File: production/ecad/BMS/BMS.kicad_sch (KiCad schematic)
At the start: 13 parts, among them J7 Conn_01x02_Pin, J8 XT60PW-M, J9 Conn_01x02_Pin, U2 AZ1117IH-3.3TRG1

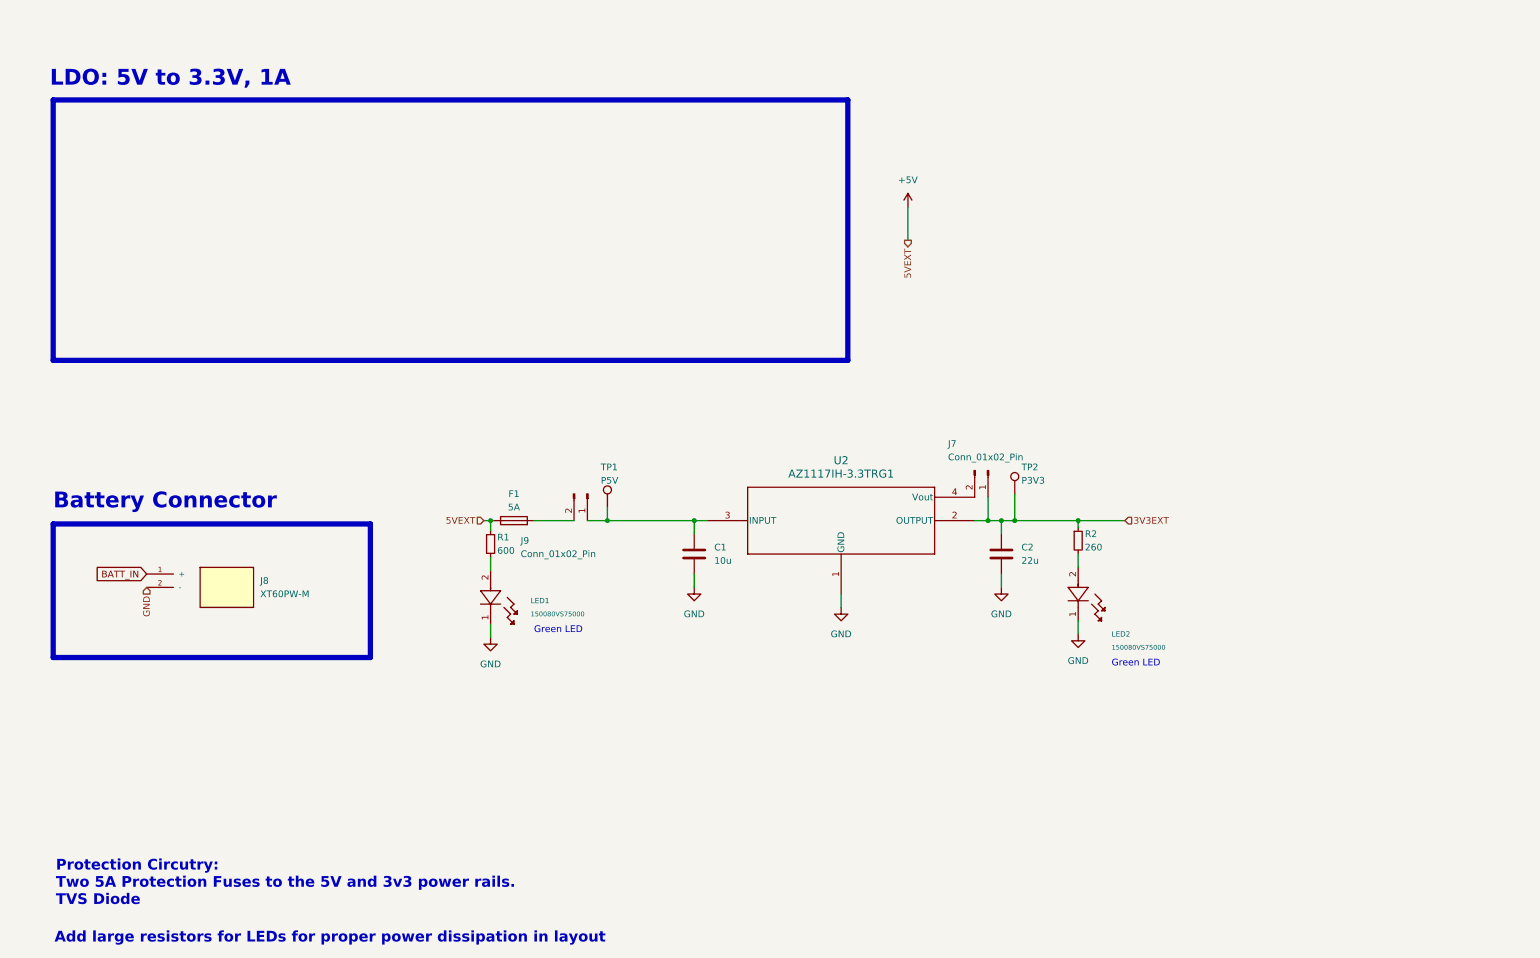
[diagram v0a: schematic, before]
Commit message: Updated LDO schematic
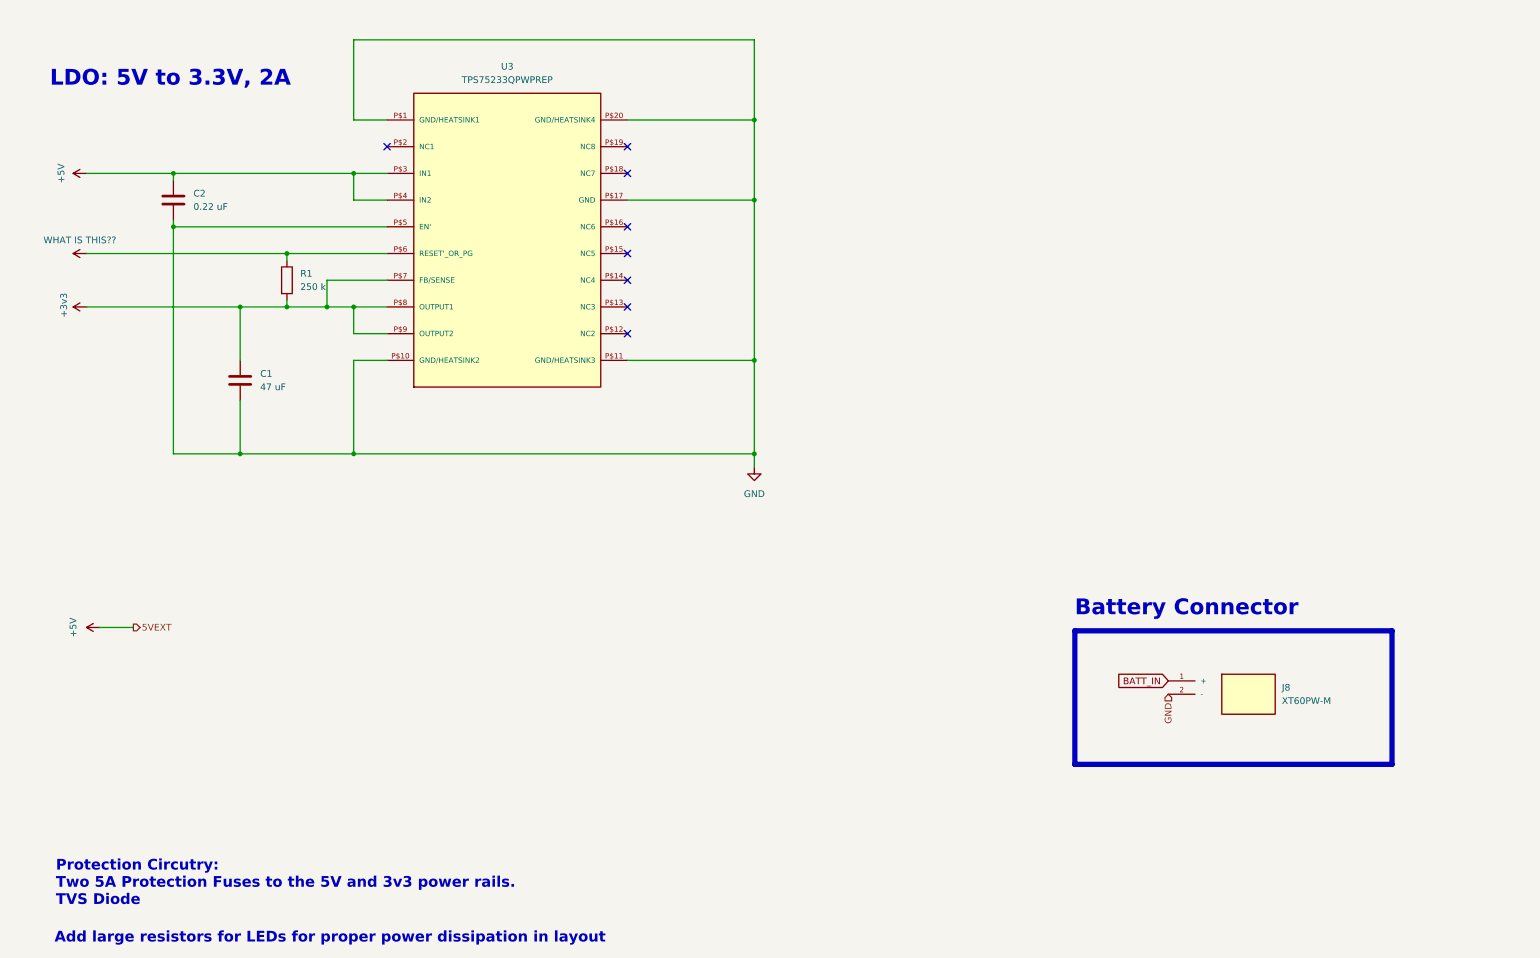
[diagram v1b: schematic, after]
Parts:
- removed F1: 5A, Fuse:Fuse_0805_2012Metric, symbol Device:Fuse
- removed J7, J9: Conn_01x02_Pin, Connector_PinHeader_2.54mm:PinHeader_1x02_P2.54mm_Vertical, symbol Connector:Conn_01x02_Pin
- removed LED1, LED2: 150080VS75000, CSTAR-MainBoard-Footprints:LED_0VS75000_WRE, symbol 2024-02-25_19-51-49:150080VS75000
- removed R1: 600, Resistor_SMD:R_0805_2012Metric, symbol Device:R_Small
- removed R2: 260, Resistor_SMD:R_0805_2012Metric, symbol Device:R_Small
- removed TP1: P5V, TestPoint:TestPoint_Pad_D2.0mm, symbol Connector:TestPoint
- removed TP2: P3V3, TestPoint:TestPoint_Pad_D2.0mm, symbol Connector:TestPoint
- removed U2: AZ1117IH-3.3TRG1, CSTAR-MainBoard-Footprints:SOT230P700X185-4N, symbol 2024-02-15_17-38-45:AZ1117IH-3.3TRG1
- added R1: 250 k, symbol Device:R
- added U3: TPS75233QPWPREP, TPS75233QPWPREP:TPS75233QPWPREP, symbol TPS75233QPWPREP:TPS75233QPWPREP
- C1: value 10u -> 47 uF; footprint Capacitor_SMD:C_0805_2012Metric -> (none)
- C2: value 22u -> 0.22 uF; footprint Capacitor_SMD:C_0805_2012Metric -> (none)
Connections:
- net 3V3EXT is gone; now on net +5V: C2.1
- net +5V: now also U3.P$3 (IN1), U3.P$4 (IN2)
- net GND: now also U3.P$1 (GND/HEATSINK1), U3.P$10 (GND/HEATSINK2), U3.P$11 (GND/HEATSINK3), U3.P$17 (GND), U3.P$20 (GND/HEATSINK4), U3.P$5 (EN')
- net +3v3: now reaches C1.1
- net +3v3: now also R1.2, U3.P$7 (FB/SENSE), U3.P$8 (OUTPUT1), U3.P$9 (OUTPUT2)
- new net WHAT IS THIS??: R1.1, U3.P$6 (RESET'_OR_PG)
- no-connect marks 0 -> 8
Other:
- note added: "LDO: 5V to 3.3V, 2A"
- note removed: "Green LED"
- note removed: "LDO: 5V to 3.3V, 1A"
- moved on the sheet: J8

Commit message: updated pullup resistors
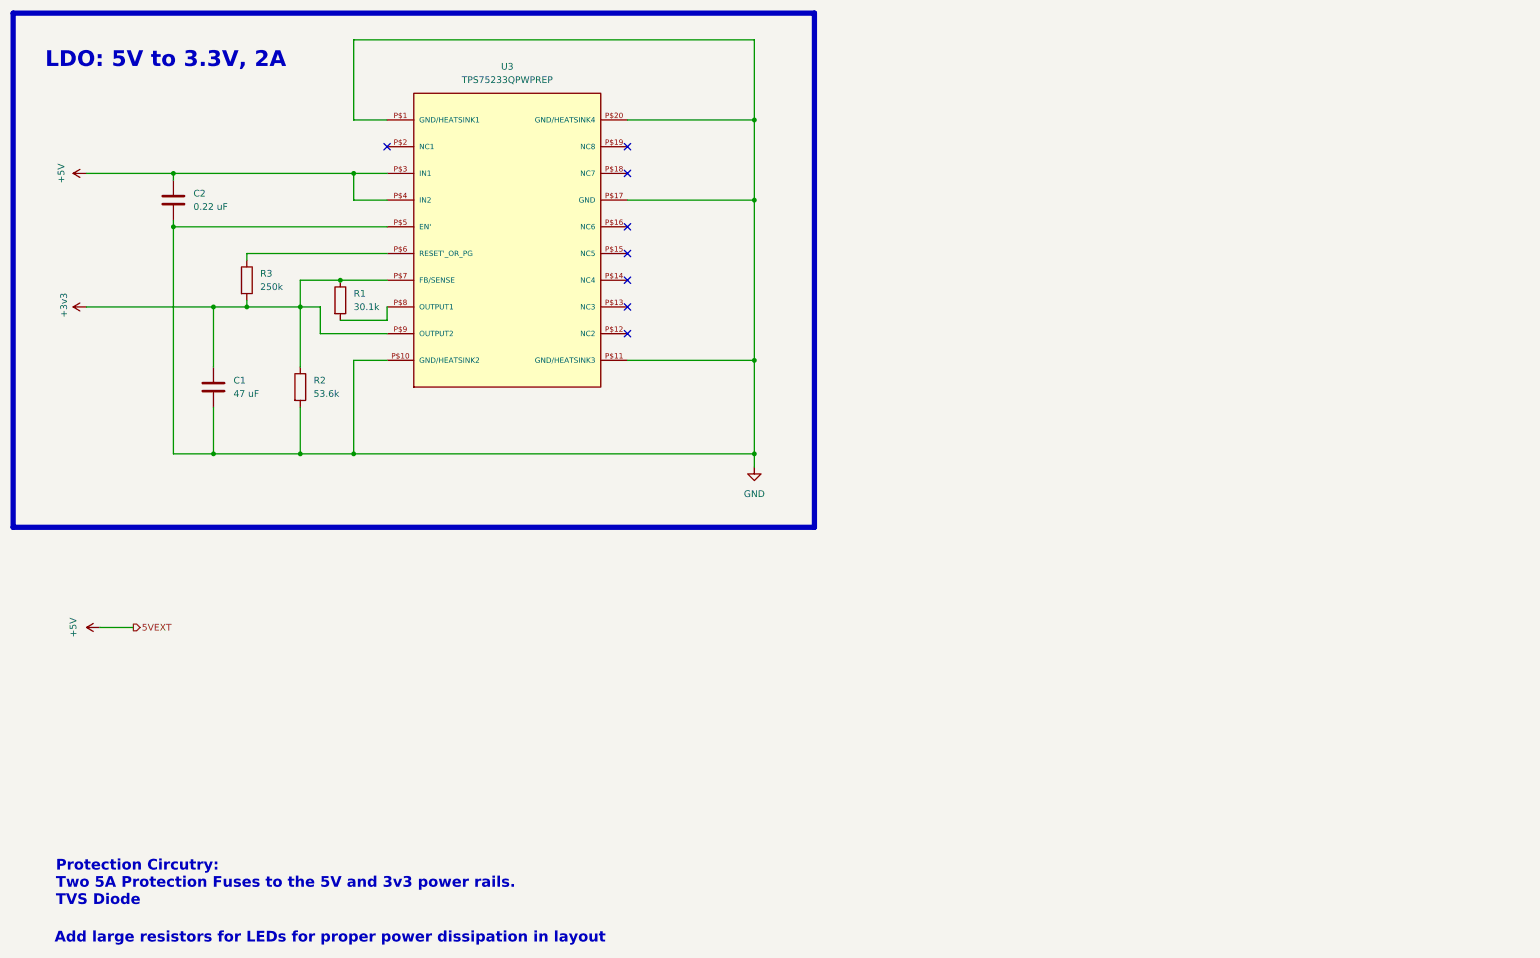
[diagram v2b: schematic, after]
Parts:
- removed J8: XT60PW-M, CSTAR-MainBoard-Footprints:AMASS_XT60PW-M, symbol XT60PW-M:XT60PW-M
- added R1: 30.1k, symbol Device:R
- added R2: 53.6k, symbol Device:R
- R3: renamed from R1; value 250 k -> 250k
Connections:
- net +3v3: now also R1.1, R2.1; no longer U3.P$8 (OUTPUT1)
- net GND: now also R2.2
- net WHAT IS THIS??: no longer names the net of R3.1, U3.P$6 (RESET'_OR_PG)
- new net: R1.2, U3.P$8 (OUTPUT1)
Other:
- note removed: "Battery Connector"
- moved on the sheet: C1, R3

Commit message: erc check
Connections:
- net +3v3 renamed +3V3

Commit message: barreljack
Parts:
- added J7: ADC-028-1-T/R-PA10T, ADC-028-x-T/R-PA10T_ADM, symbol 2024-10-20_20-22-38:ADC-028-1-T_R-PA10T
- R1: value 30.1k -> 53.6k
- R2: value 53.6k -> 30.1k
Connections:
- net +3V3: now also R1.2, U3.P$8 (OUTPUT1)
- net +5V: now also J7.2
- net GND: now also J7.1A
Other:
- note added: "Barrel jack connector: 5V from wall adapter"
- moved on the sheet: C1, C2, R1, R2, R3, U3

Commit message: erc
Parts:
- renumbered R3 to R8, U3 to U4
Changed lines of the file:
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@@
 		(dnp no)
 		(fields_autoplaced yes)
-		(property "Reference" "R3"
+		(property "Reference" "R8"
 			(at 71.12 66.0399 0)
 			(effects
@@
 			(project "Main"
 				(path "/a34d77bc-8f6a-417e-a206-3165e6c5c658/8907b1b2-1248-4544-8d7d-33764869f691"
-					(reference "R3")
+					(reference "R8")
 					(unit 1)
 				)
@@
 		(dnp no)
 		(fields_autoplaced yes)
-		(property "Reference" "U3"
+		(property "Reference" "U4"
 			(at 118.11 26.67 0)
 			(effects
@@
 			(project "Main"
 				(path "/a34d77bc-8f6a-417e-a206-3165e6c5c658/8907b1b2-1248-4544-8d7d-33764869f691"
-					(reference "U3")
+					(reference "U4")
 					(unit 1)
 				)

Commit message: Stylistic changes made
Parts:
- added R10, R9: 0, symbol Device:R
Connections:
- net +5V: now also J7.3, R10.2; no longer J7.2
- net GND: now also R9.2; no longer U4.P$1 (GND/HEATSINK1), U4.P$5 (EN')
- net at J7.1B: now also R9.1
- new net: J7.2, R10.1

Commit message: Stylistic edits made
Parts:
- renumbered R10 to DNP
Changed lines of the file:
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@@
 	(hierarchical_label "5VEXT"
 		(shape input)
-		(at 38.1 46.99 180)
+		(at 196.85 99.06 180)
 		(fields_autoplaced yes)
 		(effects
@@
 	(hierarchical_label "3V3EXT"
 		(shape input)
-		(at 38.1 72.39 180)
+		(at 196.85 105.41 180)
 		(fields_autoplaced yes)
 		(effects
@@
 		)
 	)
-	(hierarchical_label "5VEXT"
+	(hierarchical_label "GND"
 		(shape input)
-		(at 196.85 99.06 180)
+		(at 199.39 85.09 180)
 		(fields_autoplaced yes)
 		(effects
@@
 		)
 	)
-	(hierarchical_label "3V3EXT"
-		(shape input)
-		(at 196.85 105.41 180)
-		(fields_autoplaced yes)
-		(effects
-			(font
-				(size 1.27 1.27)
-			)
-			(justify right)
-		)
-	)
-	(hierarchical_label "GND"
-		(shape input)
-		(at 199.39 85.09 180)
-		(fields_autoplaced yes)
-		(effects
-			(font
-				(size 1.27 1.27)
-			)
-			(justify right)
-		)
-	)
 	(symbol
 		(lib_id "2024-10-20_20-22-38:ADC-028-1-T_R-PA10T")
@@
 	)
 	(symbol
+		(lib_id "power:+3V3")
+		(at 38.1 72.39 0)
+		(unit 1)
+		(exclude_from_sim no)
+		(in_bom yes)
+		(on_board yes)
+		(dnp no)
+		(fields_autoplaced yes)
+		(property "Reference" "#PWR045"
+			(at 38.1 76.2 0)
+			(effects
+				(font
+					(size 1.27 1.27)
+				)
+				(hide yes)
+			)
+		)
+		(property "Value" "+3V3"
+			(at 40.64 71.1199 0)
+			(effects
+				(font
+					(size 1.27 1.27)
+				)
+				(justify left)
+			)
+		)
+		(property "Footprint" ""
+			(at 38.1 72.39 0)
+			(effects
+				(font
+					(size 1.27 1.27)
+				)
+				(hide yes)
+			)
+		)
+		(property "Datasheet" ""
+			(at 38.1 72.39 0)
+			(effects
+				(font
+					(size 1.27 1.27)
+				)
+				(hide yes)
+			)
+		)
+		(property "Description" "Power symbol creates a global label with name \"+3V3\""
+			(at 38.1 72.39 0)
+			(effects
+				(font
+					(size 1.27 1.27)
+				)
+				(hide yes)
+			)
+		)
+		(pin "1"
+		)
+		(instances
+			(project "Main"
+				(path "/a34d77bc-8f6a-417e-a206-3165e6c5c658/8907b1b2-1248-4544-8d7d-33764869f691"
+					(reference "#PWR045")
+					(unit 1)
+				)
+			)
+		)
+	)
+	(symbol
 		(lib_id "power:GND")
 		(at 90.17 82.55 0)
@@
 		(on_board yes)
 		(dnp no)
-		(property "Reference" "R10"
+		(property "Reference" "DNP"
 			(at 231.394 48.006 90)
 			(effects
@@
 			(project "Main"
 				(path "/a34d77bc-8f6a-417e-a206-3165e6c5c658/8907b1b2-1248-4544-8d7d-33764869f691"
-					(reference "R10")
-					(unit 1)
-				)
+					(reference "DNP")
+					(unit 1)
+				)
+			)
+		)
+	)
+	(symbol
+		(lib_id "power:+5V")
+		(at 38.1 46.99 0)
+		(unit 1)
+		(exclude_from_sim no)
+		(in_bom yes)
+		(on_board yes)
+		(dnp no)
+		(fields_autoplaced yes)
+		(property "Reference" "#PWR044"
+			(at 38.1 50.8 0)
+			(effects
+				(font
+					(size 1.27 1.27)
+				)
+				(hide yes)
+			)
+		)
+		(property "Value" "+5V"
+			(at 40.64 45.7199 0)
+			(effects
+				(font
+					(size 1.27 1.27)
+				)
+				(justify left)
+			)
+		)
+		(property "Footprint" ""
+			(at 38.1 46.99 0)
+			(effects
+				(font
+					(size 1.27 1.27)
+				)
+				(hide yes)
+			)
+		)
+		(property "Datasheet" ""
+			(at 38.1 46.99 0)
+			(effects
+				(font
+					(size 1.27 1.27)
+				)
+				(hide yes)
+			)
+		)
+		(property "Description" "Power symbol creates a global label with name \"+5V\""
+			(at 38.1 46.99 0)
+			(effects
+				(font
+					(size 1.27 1.27)
+				)
+				(hide yes)
+			)
+		)
+		(pin "1"
+		)
+		(instances
+			(project "Main"
+				(path "/a34d77bc-8f6a-417e-a206-3165e6c5c658/8907b1b2-1248-4544-8d7d-33764869f691"
+					(reference "#PWR044")
+					(unit 1)
+				)

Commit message: BMS fixed
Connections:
- net GND: now also U4.P$1 (GND/HEATSINK1), U4.P$5 (EN')
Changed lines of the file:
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@@
+	)
+	(symbol
+		(lib_id "power:GND")
+		(at 90.17 57.15 0)
+		(unit 1)
+		(exclude_from_sim no)
+		(in_bom yes)
+		(on_board yes)
+		(dnp no)
+		(property "Reference" "#PWR049"
+			(at 90.17 63.5 0)
+			(effects
+				(font
+					(size 1.27 1.27)
+				)
+				(hide yes)
+			)
+		)
+		(property "Value" "GND"
+			(at 87.884 60.198 0)
+			(effects
+				(font
+					(size 1.27 1.27)
+				)
+			)
+		)
+		(property "Footprint" ""
+			(at 90.17 57.15 0)
+			(effects
+				(font
+					(size 1.27 1.27)
+				)
+				(hide yes)
+			)
+		)
+		(property "Datasheet" ""
+			(at 90.17 57.15 0)
+			(effects
+				(font
+					(size 1.27 1.27)
+				)
+				(hide yes)
+			)
+		)
+		(property "Description" "Power symbol creates a global label with name \"GND\" , ground"
+			(at 90.17 57.15 0)
+			(effects
+				(font
+					(size 1.27 1.27)
+				)
+				(hide yes)
+			)
+		)
+		(pin "1"
+		)
+		(instances
+			(project "Main"
+				(path "/a34d77bc-8f6a-417e-a206-3165e6c5c658/8907b1b2-1248-4544-8d7d-33764869f691"
+					(reference "#PWR049")
+					(unit 1)
+				)
+			)
+		)
 	)
 	(symbol
@@
 					(unit 1)
 				)
+			)
+		)
+	)
+	(symbol
+		(lib_id "power:GND")
+		(at 90.17 36.83 0)
+		(unit 1)
+		(exclude_from_sim no)
+		(in_bom yes)
+		(on_board yes)
+		(dnp no)
+		(fields_autoplaced yes)
+		(property "Reference" "#PWR048"
+			(at 90.17 43.18 0)
+			(effects
+				(font
+					(size 1.27 1.27)
+				)
+				(hide yes)
+			)
+		)
+		(property "Value" "GND"
+			(at 90.17 41.91 0)
+			(effects
+				(font
+					(size 1.27 1.27)
+				)
+			)
+		)
+		(property "Footprint" ""
+			(at 90.17 36.83 0)
+			(effects
+				(font
+					(size 1.27 1.27)
+				)
+				(hide yes)
+			)
+		)
+		(property "Datasheet" ""
+			(at 90.17 36.83 0)
+			(effects
+				(font
+					(size 1.27 1.27)
+				)
+				(hide yes)
+			)
+		)
+		(property "Description" "Power symbol creates a global label with name \"GND\" , ground"
+			(at 90.17 36.83 0)
+			(effects
+				(font
+					(size 1.27 1.27)
+				)
+				(hide yes)
+			)
+		)
+		(pin "1"
+		)
+		(instances
+			(project "Main"
+				(path "/a34d77bc-8f6a-417e-a206-3165e6c5c658/8907b1b2-1248-4544-8d7d-33764869f691"
+					(reference "#PWR048")
+					(unit 1)
+				)
